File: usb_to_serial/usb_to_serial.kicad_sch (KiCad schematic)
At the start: 25 parts, among them J1 USB4105-GF-A, J2 RJ45_LED_Shielded, U1 FT232RL, U2 MAX3243CDBR

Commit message: Revision for Aisler design rules
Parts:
- C11, C5, C9: value 100nF -> 330nF
- C7: value 100nF -> 47nF
- R1, R2: value 4.7K -> 5.1K

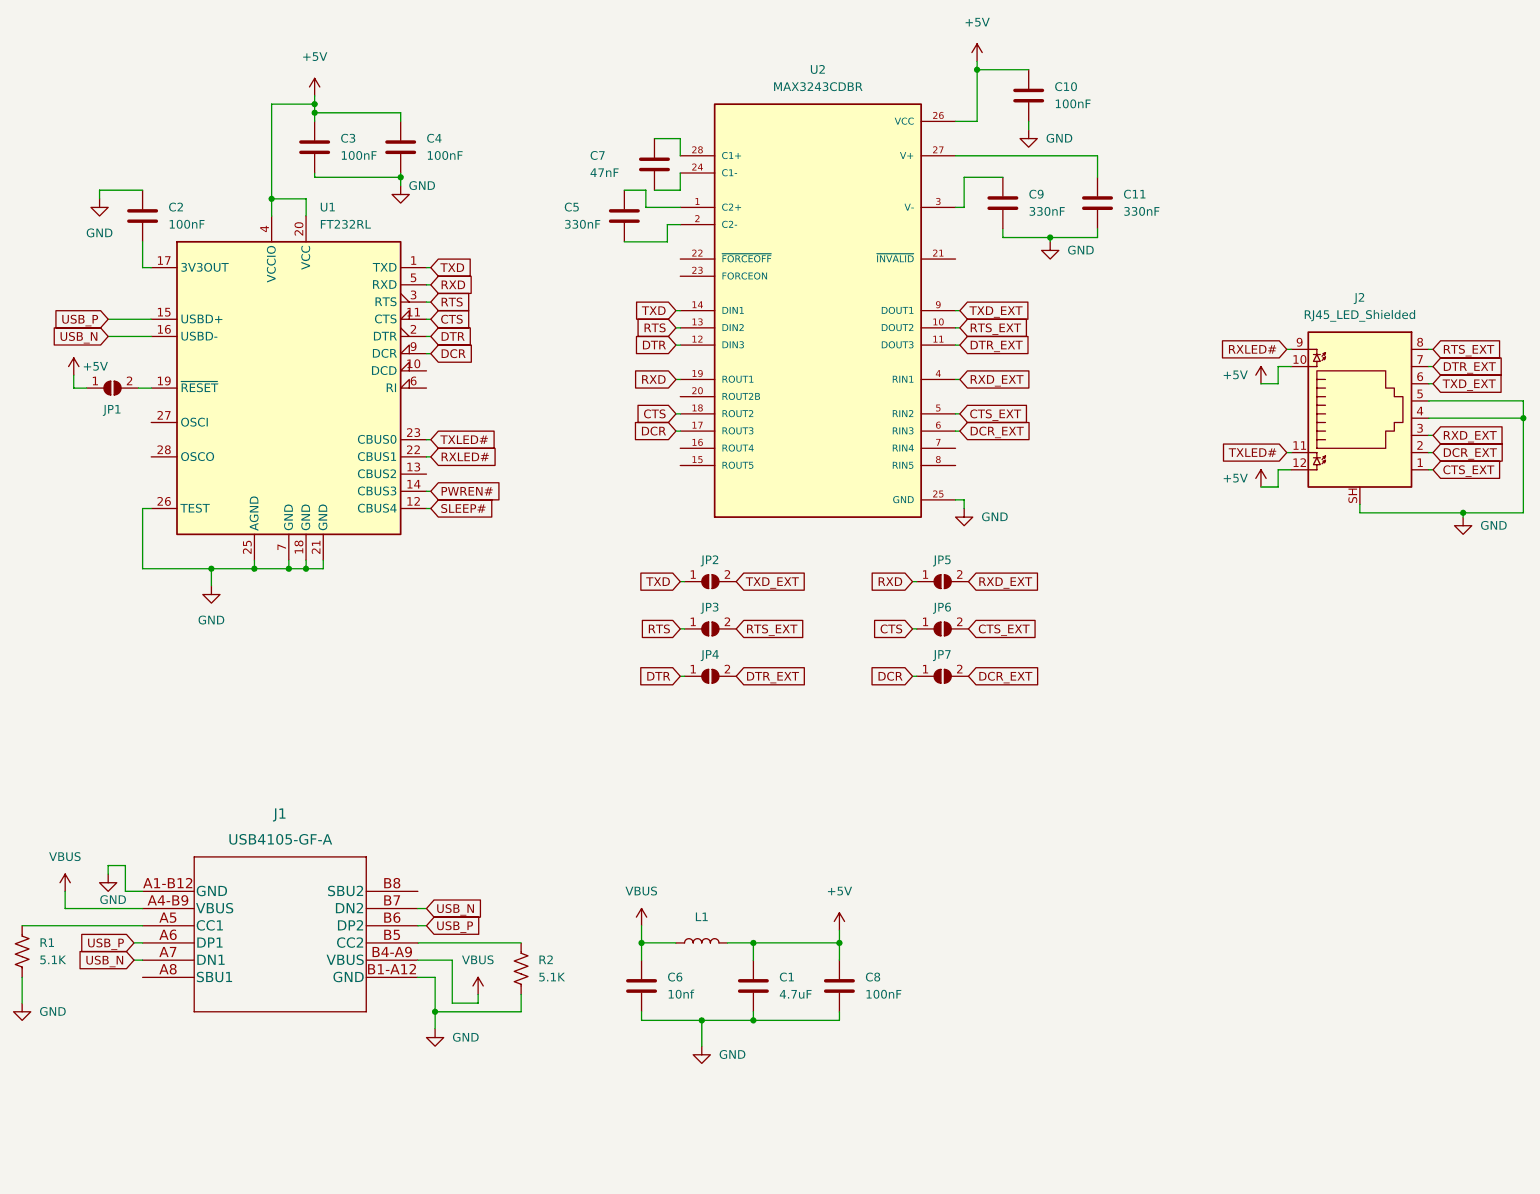
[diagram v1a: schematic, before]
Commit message: Change USB-C connector footprint with one with NPTHs, add connections for forceon/forceoff on MAX3243
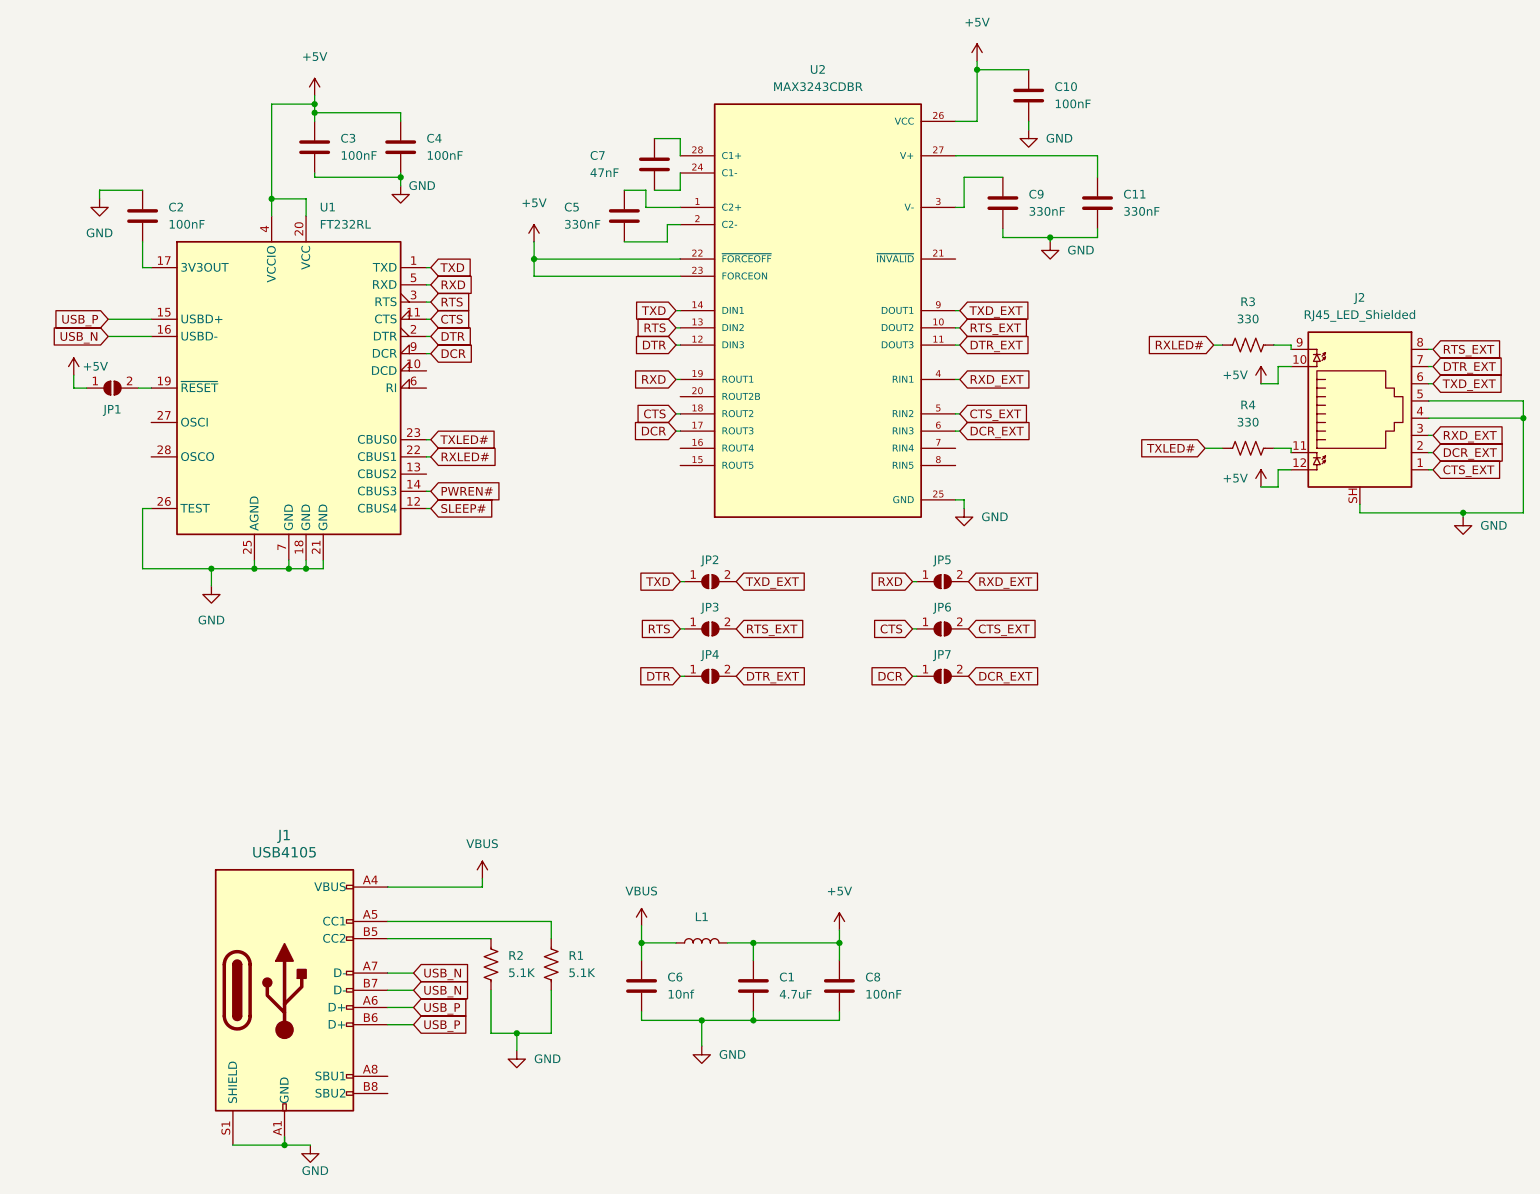
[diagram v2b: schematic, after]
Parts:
- added R3, R4: 330, Resistor_SMD:R_0603_1608Metric_Pad0.98x0.95mm_HandSolder, symbol Device:R_US
- J1: value USB4105-GF-A -> USB4105; footprint Personal:USB4105-GF-A -> Connector_USB:USB_C_Receptacle_HRO_TYPE-C-31-M-12; symbol CustomSymbols:USB4105-GF-A -> Connector:USB_C_Receptacle_USB2.0_16P; MANUFACTURER (none) -> Global Connector Technology; MAXIMUM_PACKAGE_HEIGHT (none) -> 3.31mm; PARTREV (none) -> B3; STANDARD (none) -> Manufacturer Recommendations
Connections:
- net +5V: now also U2.22 (~{FORCEOFF}), U2.23 (FORCEON)
- net GND: now also J1.A1 (GND), J1.A12 (GND), J1.B1 (GND), J1.B12 (GND), J1.S1 (SHIELD); no longer J1.A1-B12 (GND), J1.B1-A12 (GND)
- net RXLED#: now also R3.1; no longer J2.9
- net TXLED#: now also R4.1; no longer J2.11
- net VBUS: now also J1.A4 (VBUS), J1.A9 (VBUS), J1.B4 (VBUS), J1.B9 (VBUS); no longer J1.A4-B9 (VBUS), J1.B4-A9 (VBUS)
- new net: J2.11, R4.2
- new net: J2.9, R3.2
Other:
- moved on the sheet: R2
